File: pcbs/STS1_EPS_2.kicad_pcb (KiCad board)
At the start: 6 copper layers, 81 x 85 mm, 158 parts, among them J1 DS1, J2 DS2, J5 RBF, J6 Antenna Deployment, J7 Inter-EPS, J9 Battery Pack, Q1 2N7002, Q10 2N7002, Q11 2N7002, Q14 2N7002, Q15 2N7002, Q18 2N7002, Q19 2N7002, Q2 SI7272DP-T1-GE3, Q20 2N7002, Q21 SI7272DP-T1-GE3, Q22 SI7272DP-T1-GE3, Q3 2N7002, Q5 SI7135DP-T1-GE3, Q6 2N7002, Q7 2N7002, U1 4072, U11 LTC4451AV#TRMPBF, U12 LTC4451AV#TRMPBF, U13 4082, U2 LTC6995IDCB-1, U3 TPS2420RSAT, U4 MIC841H, U5 MIC841H, U6 TPS2420RSAT, U7 BQ29209DRBT, U8 4072, U9 BD50GA5WEFJ

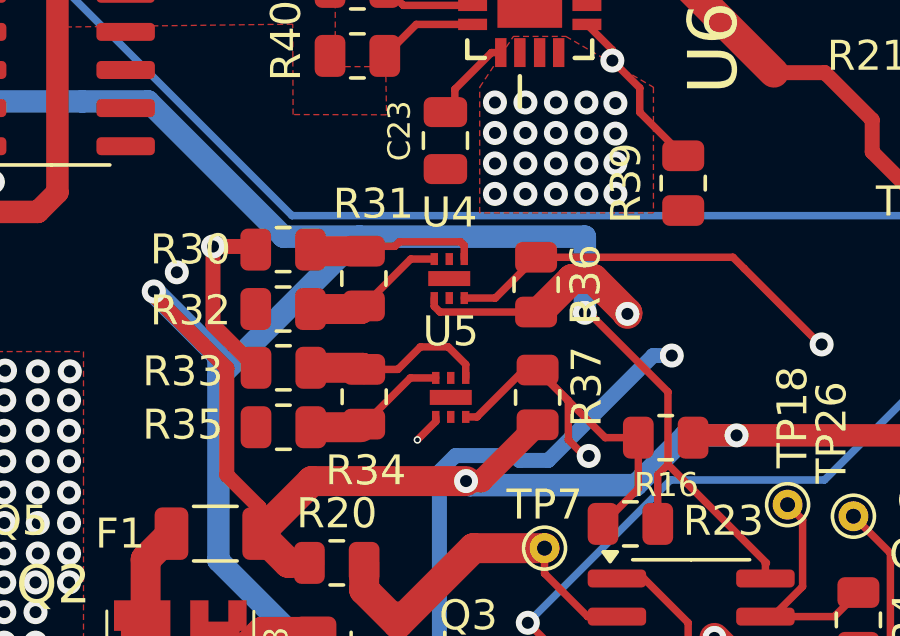
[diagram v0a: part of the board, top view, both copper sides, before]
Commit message: * New symbol for U4 and U5 on STS1_EPS_2. * Made the tracing for U4 and U5 a bit better.
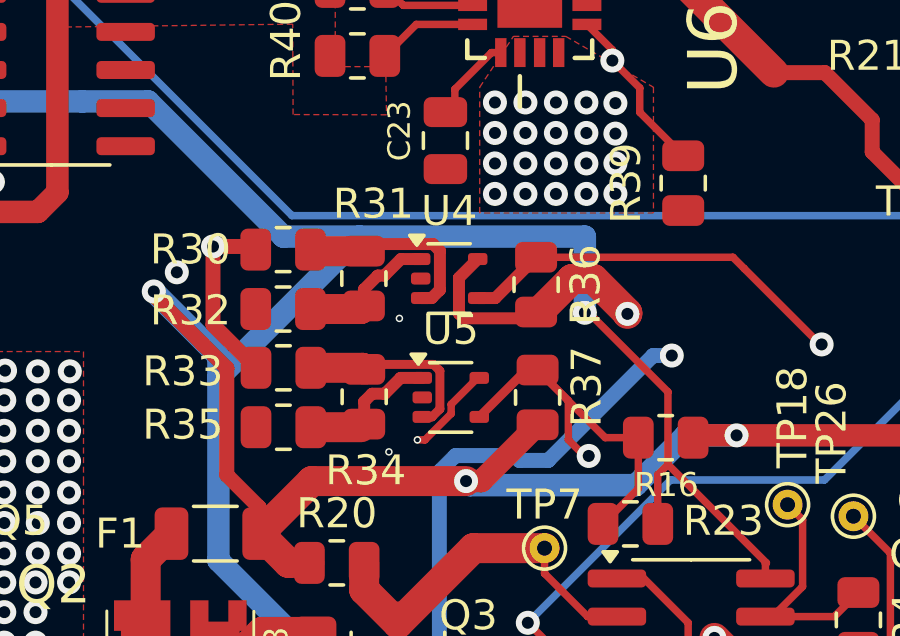
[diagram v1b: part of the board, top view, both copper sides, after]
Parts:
- U4, U5: footprint STS_Package_DFN_QFN:TDFN-6 -> Package_TO_SOT_SMD:SOT-353_SC-70-5
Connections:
- U4 pad 1: Net-(U4-LTH) -> Net-(U4-HTH)
- U4 pad 3: Net-(U4-HTH) -> Net-(U4-LTH)
- U4 pad 4: +5V -> /EPS_BAT_GOOD
- U4 pad 5: unconnected-(U4-NC-Pad5) -> +5V
- U5 pad 1: Net-(U5-LTH) -> Net-(U5-HTH)
- U5 pad 3: Net-(U5-HTH) -> Net-(U5-LTH)
- U5 pad 4: /V_LOGIC -> /UVLO_SIGNAL
- U5 pad 5: unconnected-(U5-NC-Pad5) -> /V_LOGIC
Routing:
- net /V_LOGIC: track 376.7 -> 378.8 mm
- net +5V: track 82.3 -> 83.3 mm
- net Net-(U4-LTH): track 5.78 -> 6.58 mm
- net GND: vias 30 -> 32

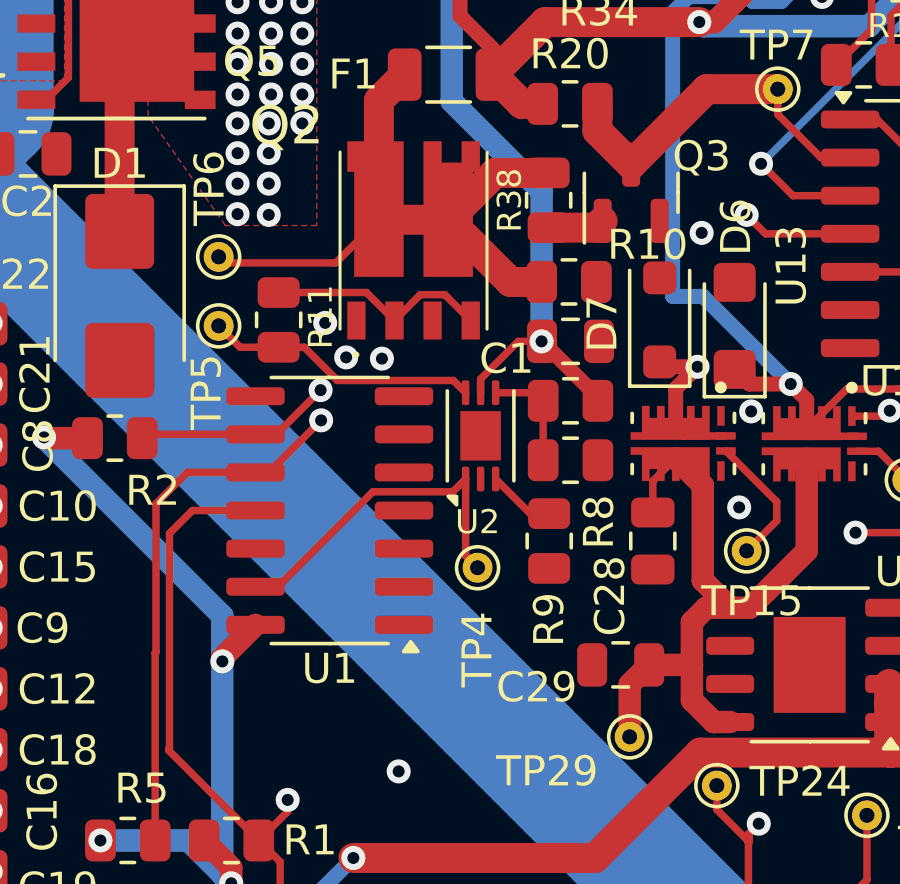
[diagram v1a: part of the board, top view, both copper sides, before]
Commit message: Fixed deployment timer symbol having wrong pin numbers.
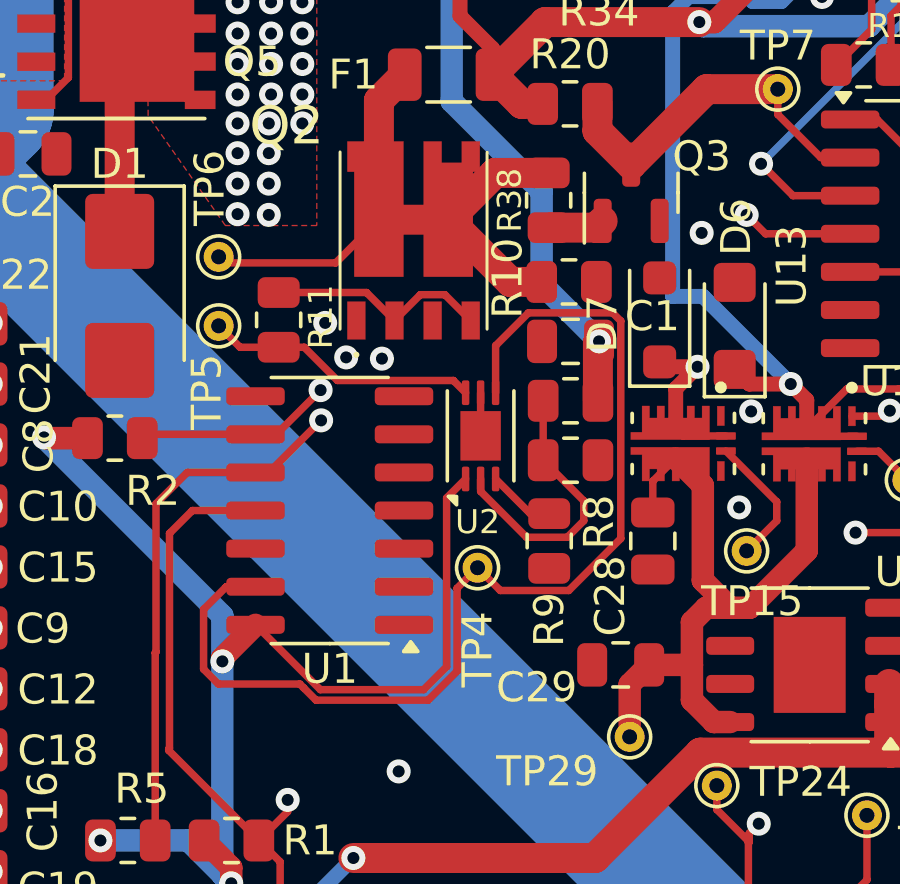
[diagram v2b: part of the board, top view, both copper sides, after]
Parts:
- turned C1 to 180 degrees
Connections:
- U2 pad 1: Net-(U2-RST/~{RST}) -> /V_LOGIC
- U2 pad 2: GND -> /Deployment Timer/DIV
- U2 pad 4: /Deployment Timer/DIV -> Net-(U2-RST/~{RST})
- U2 pad 5: /V_LOGIC -> GND
- U2 pad 7: (no net) -> GND
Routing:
- net Net-(U2-RST/~{RST}): track 11.6 -> 37.2 mm
- net /V_LOGIC: track 378.8 -> 389.9 mm
- net /Deployment Timer/DIV: track 3.68 -> 9.65 mm
- net GND: track 10.3 -> 11.8 mm

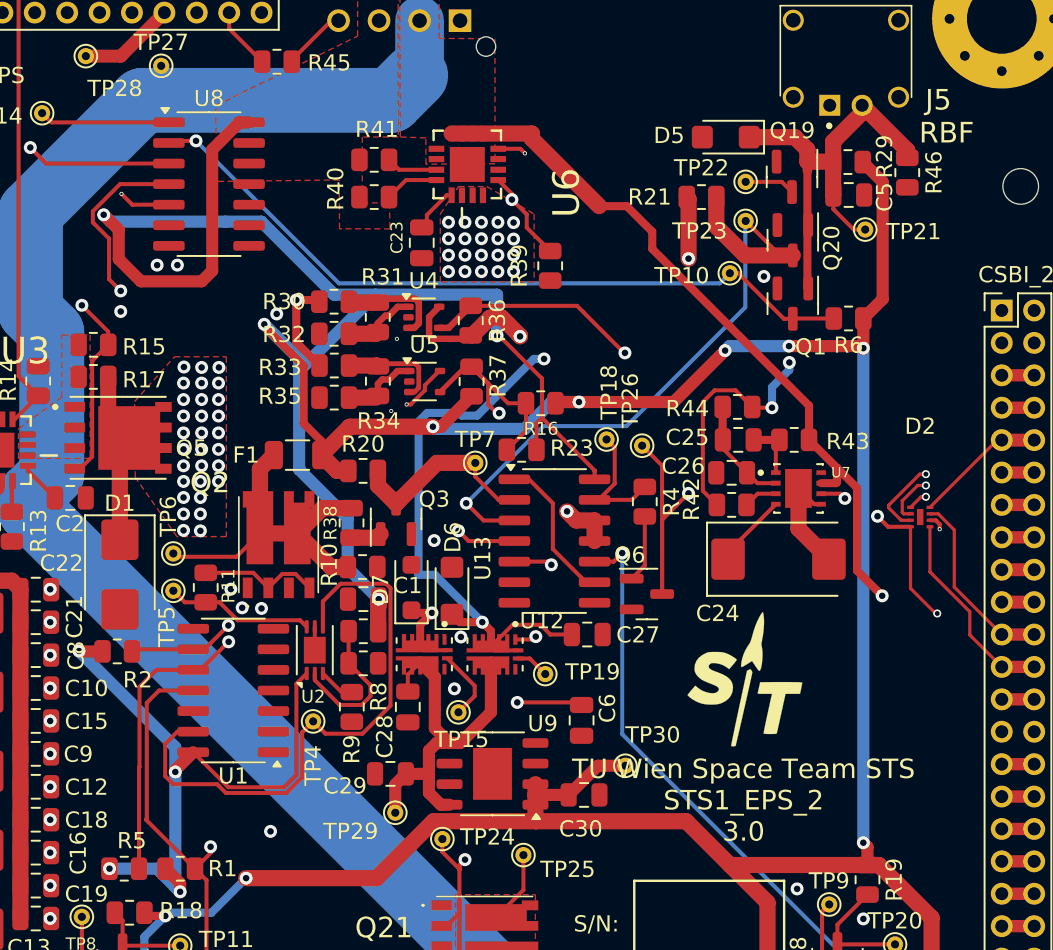
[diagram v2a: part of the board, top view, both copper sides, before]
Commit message: Fixed layout after changes to inhibit logic.
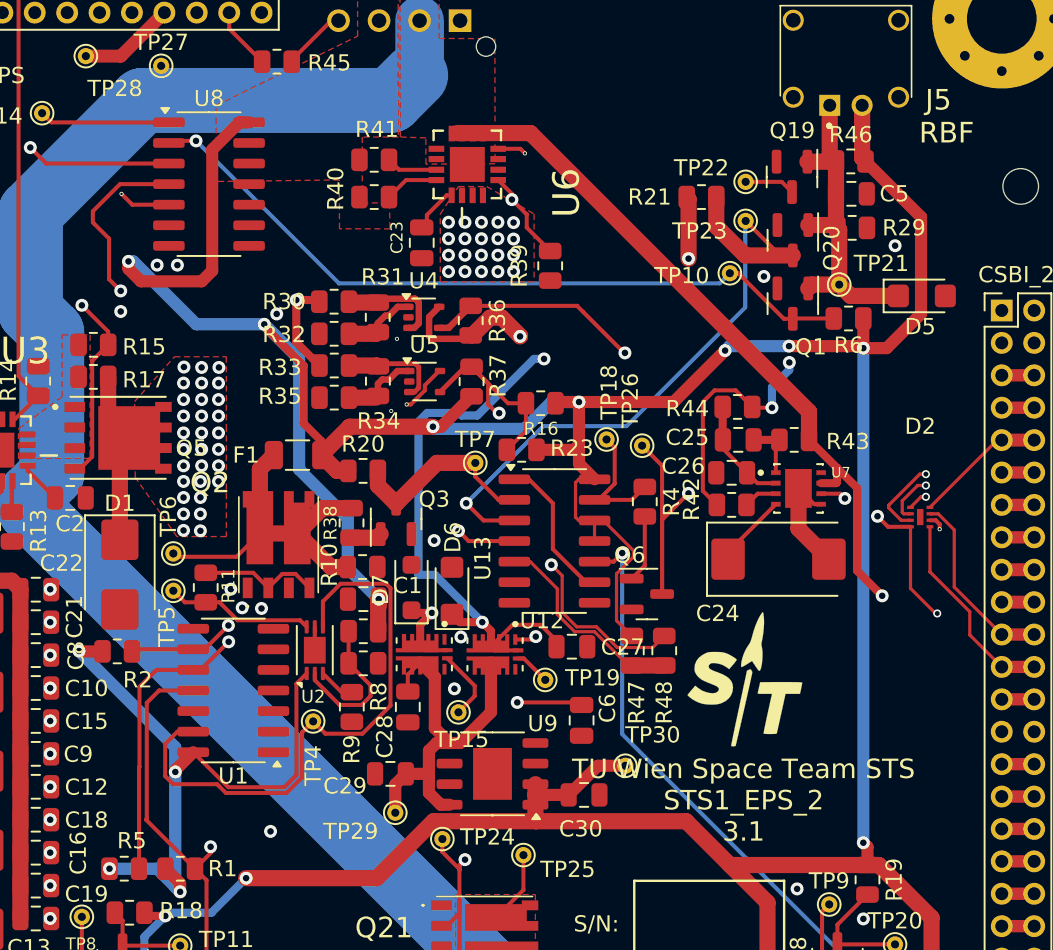
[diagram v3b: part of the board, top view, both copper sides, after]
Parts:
- added R47: 0, Resistor_SMD:R_0805_2012Metric, F.Cu at (169.8, 85.3)
- added R48: 0, Resistor_SMD:R_0805_2012Metric, F.Cu at (171.8, 85.3)
- moved D5 15.6 mm to (187.7, 63.4), turned to 0 degrees
- moved R29 4.07 mm to (183.4, 59.2), turned to 0 degrees
- moved TP21 3.76 mm to (182.6, 62.7)
- moved R46 3.55 mm to (183.3, 55.1), turned to 0 degrees
- moved C27 1.21 mm to (166.1, 85.0)
- moved TP19 0.36 mm to (164.5, 87.1)
- moved C5 0.18 mm to (183.3, 57.1)
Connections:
- C5 pad 1: /Deployment Switches + RBF/RBF+ -> /Deployment Switches + RBF/RBF-
- D5 pad 1: /Deployment Switches + RBF/RBF+ -> /Deployment Switches + RBF/RBF-
- J5 pad 1: GND -> /Deployment Switches + RBF/RBF-
- J5 pad 2: /Deployment Switches + RBF/RBF+ -> /V_LOGIC
- Q1 pad 1: /Deployment Switches + RBF/RBF+ -> /Deployment Switches + RBF/RBF-
- Q19 pad 1: /Deployment Switches + RBF/RBF+ -> /Deployment Switches + RBF/RBF-
- Q20 pad 1: /Deployment Switches + RBF/RBF+ -> /Deployment Switches + RBF/RBF-
- R29 pad 1: /V_LOGIC -> /Deployment Switches + RBF/RBF-
- R29 pad 2: /Deployment Switches + RBF/RBF+ -> GND
- R46 pad 1: /Deployment Switches + RBF/RBF+ -> /Deployment Switches + RBF/RBF-
- R46 pad 2: GND -> /V_LOGIC
- TP21 pad 1: /Deployment Switches + RBF/RBF+ -> /Deployment Switches + RBF/RBF-
- U13 pad 11: +5V -> /V_LOGIC
- U13 pad 12: +5V -> /V_LOGIC
- U13 pad 5: /UVLO_SIGNAL -> Net-(R47-Pad2)
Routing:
- net /Deployment Switches + RBF/RBF+: track 28.1 -> 0.00 mm
- net /Deployment Switches + RBF/RBF-: track 0.00 -> 20.9 mm
- net +5V: track 83.3 -> 68.1 mm, vias 2 -> 1
- net /V_LOGIC: track 389.9 -> 375.1 mm, vias 20 -> 19
- net Net-(R47-Pad2): track 0.00 -> 12.8 mm
- net /UVLO_SIGNAL: track 83.3 -> 91.9 mm
- net /BATT_RAW: track 276.5 -> 275.2 mm
- net GND: vias 32 -> 33
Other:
- board text added: "TU Wien Space Team STS STS1_EPS_2 3.1"
- board text removed: "TU Wien Space Team STS STS1_EPS_2 3.0"

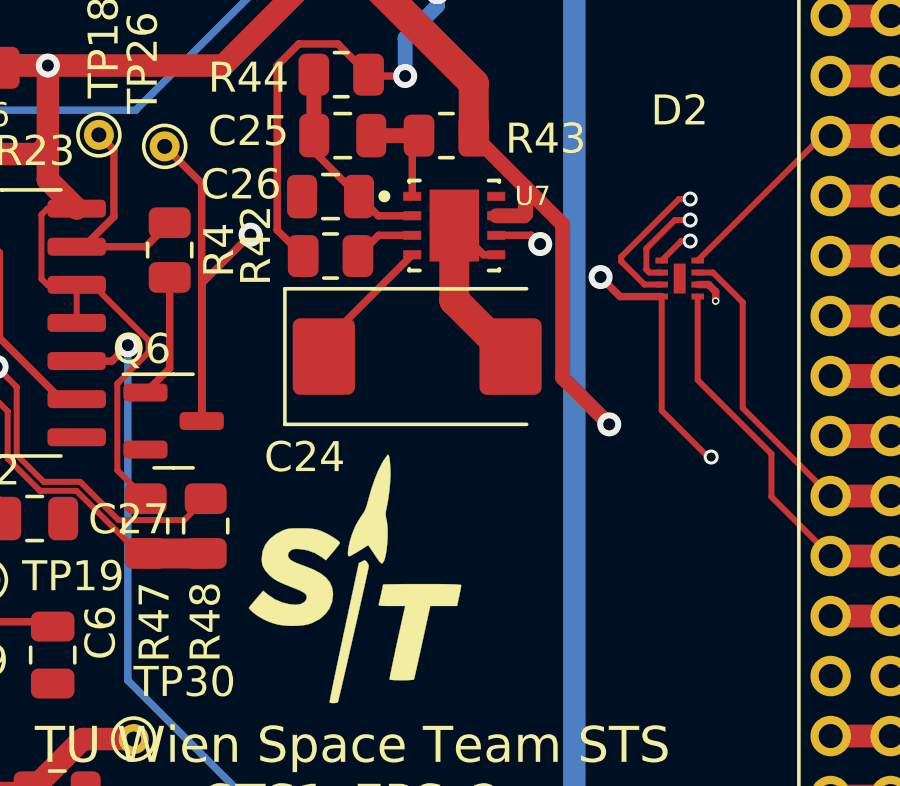
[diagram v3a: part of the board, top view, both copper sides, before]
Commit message: * Cell balancer is now deactivated by UVLO signal, rather than bat fault signal * Bat Fault signal is now an open drain output
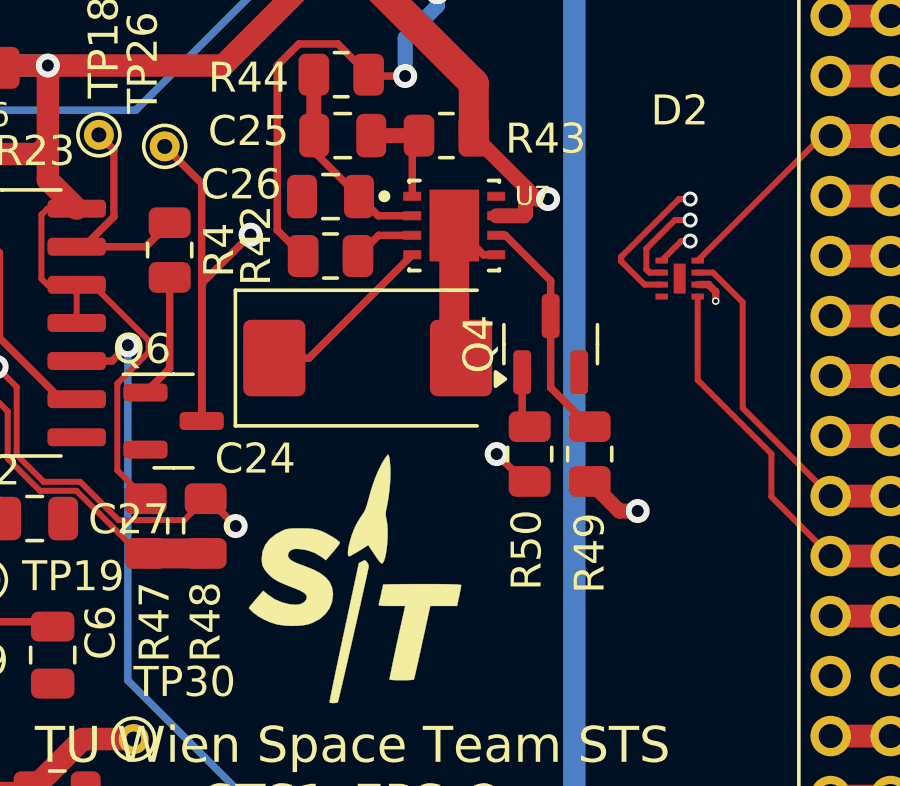
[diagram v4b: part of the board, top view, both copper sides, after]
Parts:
- added Q4: 2N7002, Package_TO_SOT_SMD:SOT-23, F.Cu at (183.3, 79.2)
- added R49: 100k, Resistor_SMD:R_0805_2012Metric, F.Cu at (184.6, 82.9)
- added R50: 100, Resistor_SMD:R_0805_2012Metric, F.Cu at (182.6, 82.9)
- U4: value MIC841H -> MIC841N
- moved C24 1.65 mm to (177.2, 79.7)
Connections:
- net /Battery/~{BATT_INHIBIT} renamed /Battery/BATT_INHIBIT
- CSBI_2 pad 19: /BAT_FAULT -> Net-(CSBI_2-Pin_19)
- CSBI_2 pad 20: /BAT_FAULT -> Net-(CSBI_2-Pin_19)
- D2 pad 4: /BAT_FAULT -> unconnected-(D2-Pad4)
- U7 pad 6: /BAT_FAULT -> Net-(Q4-D)
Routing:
- net /BAT_FAULT: track 18.7 -> 0.00 mm, vias 3 -> 0
- net /V_LOGIC: track 375.1 -> 390.3 mm, vias 19 -> 20
- net /BATT_RAW: track 275.2 -> 261.9 mm
- net /UVLO_SIGNAL: track 91.9 -> 104.9 mm, vias 3 -> 5
- net Net-(Q4-D): track 0.00 -> 7.85 mm
- net Net-(CSBI_2-Pin_19): track 0.00 -> 2.00 mm
- net Net-(Q4-G): track 0.00 -> 1.92 mm
- net Net-(U7-CD): track 4.61 -> 6.02 mm
- net GND: track 11.8 -> 11.2 mm

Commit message: Fixed inhibit logic, again...
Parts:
- added R51: 0, Resistor_SMD:R_0805_2012Metric, F.Cu at (139.4, 90.6)
- U1, U8: value 4072 -> 4012
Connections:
- U1 pad 12: GND -> Net-(R51-Pad2)
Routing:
- net /V_LOGIC: track 390.3 -> 398.4 mm
- net /DS1_SIGNAL_2: track 62.1 -> 67.0 mm
- net Net-(R51-Pad2): track 0.00 -> 3.60 mm
- net /RBF_SIGNAL_2: track 78.2 -> 81.0 mm
